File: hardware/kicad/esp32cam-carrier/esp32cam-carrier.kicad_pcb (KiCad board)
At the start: 2 copper layers, 78.7 x 33 mm, 14 parts, among them Q1 2N7000

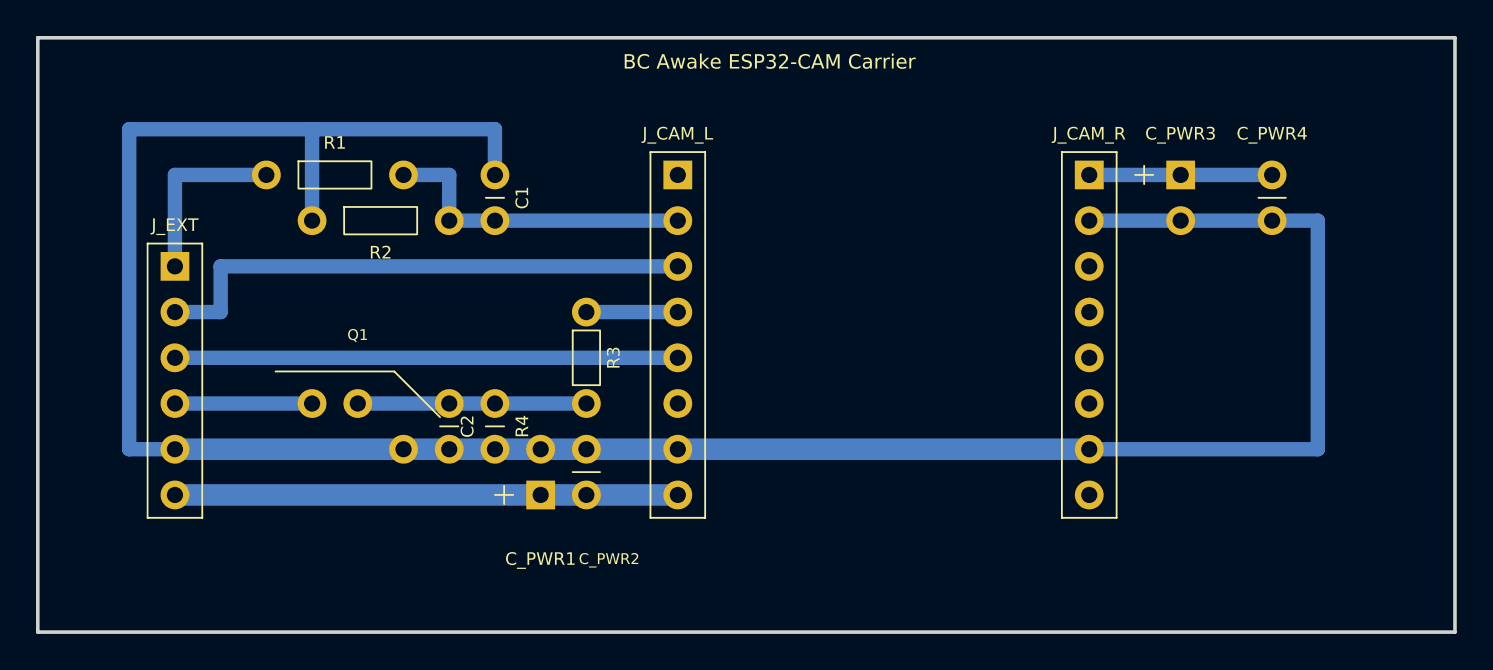
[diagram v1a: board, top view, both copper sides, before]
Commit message: fix(hardware): align ESP32-CAM carrier PCB and docs to physical pinout
- Correct ESP32-CAM ASCII header diagrams in docs/pinout.md to match physical module
- Realign J_CAM_L and J_CAM_R socket mappings and isolate IO16 (PSRAM) in scripts/generate_carrier_pcb.py
- Re-route single-layer copper B.Cu with zero track crossings and 0 DRC violations
- Update J_EXT terminal ordering and coordinate maps in docs/esp32cam-carrier-pcb.md and docs/bom.md
- Sync hardware-targets spec and archive esp32cam-prototype-pcb and fix-esp32cam-carrier-pinout changes
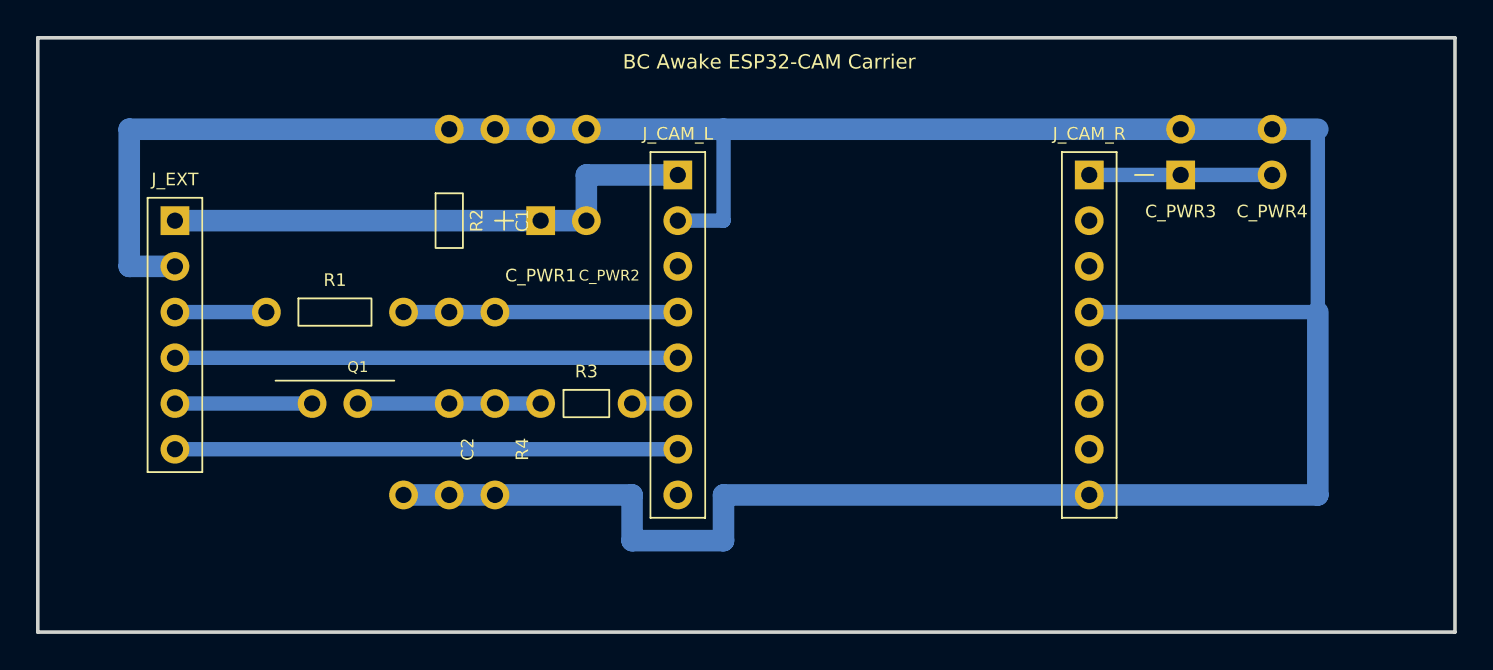
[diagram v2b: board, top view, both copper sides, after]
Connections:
- J_CAM_L pad 1: (no net) -> +5VSB
- J_CAM_L pad 2: NET_IO13 -> GND
- J_CAM_L pad 3: BTN_A -> (no net)
- J_CAM_L pad 4: NET_IO14 -> NET_IO13
- J_CAM_L pad 5: PWR_BTN# -> BTN_A
- J_CAM_L pad 6: (no net) -> NET_IO14
- J_CAM_L pad 7: GND -> PWR_BTN#
- J_CAM_L pad 8: +5VSB -> (no net)
- J_CAM_R pad 2: GND -> (no net)
- J_CAM_R pad 4: (no net) -> GND
- J_CAM_R pad 7: GND -> (no net)
- J_CAM_R pad 8: (no net) -> GND
- J_EXT pad 1: TPMS1 -> +5VSB
- J_EXT pad 2: BTN_A -> GND
- J_EXT pad 3: PWR_BTN# -> TPMS1
- J_EXT pad 4: PS_ON# -> BTN_A
- J_EXT pad 5: GND -> PS_ON#
- J_EXT pad 6: +5VSB -> PWR_BTN#
- R3 pad 1: NET_IO14 -> NET_GATE
- R3 pad 2: NET_GATE -> NET_IO14
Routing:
- net GND: track 137.2 -> 172.7 mm
- net TPMS1: track 10.2 -> 5.08 mm
- net NET_IO13: track 17.8 -> 15.2 mm
- net BTN_A: track 30.5 -> 27.9 mm
- net +5VSB: track 27.9 -> 30.5 mm
- net NET_IO14: track 5.08 -> 2.54 mm
- net NET_GATE: track 12.7 -> 10.2 mm

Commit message: fix(hardware): isolate ESP32-CAM GND/R reset pin on carrier PCB
Disconnect J_CAM_R pin 8 (GND/R) from ground to prevent holding the ESP32-CAM in hardware reset on clone boards, reroute the bottom ground bus via the left edge, and update documentation and specs.
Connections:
- J_CAM_R pad 8: GND -> (no net)
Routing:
- net GND: track 172.7 -> 139.7 mm
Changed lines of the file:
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@@
 		(pad "6" thru_hole circle (at 155.88 117.78) (size 1.6 1.6) (drill 0.9) (layers "*.Cu" "*.Mask") (net 0 ""))
 		(pad "7" thru_hole circle (at 155.88 120.32) (size 1.6 1.6) (drill 0.9) (layers "*.Cu" "*.Mask") (net 0 ""))
-		(pad "8" thru_hole circle (at 155.88 122.86) (size 1.6 1.6) (drill 0.9) (layers "*.Cu" "*.Mask") (net 1 "GND"))
+		(pad "8" thru_hole circle (at 155.88 122.86) (size 1.6 1.6) (drill 0.9) (layers "*.Cu" "*.Mask") (net 0 ""))
 	)
 	(footprint "Capacitor_THT:CP_Radial_D8.0mm_P3.50mm"
@@
 	(segment (start 168.58 102.54) (end 168.58 112.7) (width 0.8) (layer "B.Cu") (net 1))
 	(segment (start 168.58 112.7) (end 155.88 112.7) (width 0.8) (layer "B.Cu") (net 1))
-	(segment (start 168.58 112.7) (end 168.58 122.86) (width 1.2) (layer "B.Cu") (net 1))
-	(segment (start 168.58 122.86) (end 155.88 122.86) (width 1.2) (layer "B.Cu") (net 1))
-	(segment (start 155.88 122.86) (end 135.56 122.86) (width 1.2) (layer "B.Cu") (net 1))
-	(segment (start 135.56 122.86) (end 135.56 125.4) (width 1.2) (layer "B.Cu") (net 1))
-	(segment (start 135.56 125.4) (end 130.48 125.4) (width 1.2) (layer "B.Cu") (net 1))
-	(segment (start 130.48 125.4) (end 130.48 122.86) (width 1.2) (layer "B.Cu") (net 1))
-	(segment (start 130.48 122.86) (end 122.86 122.86) (width 1.2) (layer "B.Cu") (net 1))
-	(segment (start 122.86 122.86) (end 120.32 122.86) (width 1.2) (layer "B.Cu") (net 1))
-	(segment (start 120.32 122.86) (end 117.78 122.86) (width 1.2) (layer "B.Cu") (net 1))
+	(segment (start 102.54 110.16) (end 102.54 122.86) (width 1.2) (layer "B.Cu") (net 1))
+	(segment (start 102.54 122.86) (end 117.78 122.86) (width 1.2) (layer "B.Cu") (net 1))
+	(segment (start 117.78 122.86) (end 120.32 122.86) (width 1.2) (layer "B.Cu") (net 1))
+	(segment (start 120.32 122.86) (end 122.86 122.86) (width 1.2) (layer "B.Cu") (net 1))
 	(segment (start 105.08 112.7) (end 110.16 112.7) (width 0.8) (layer "B.Cu") (net 4))
 	(segment (start 117.78 112.7) (end 120.32 112.7) (width 0.8) (layer "B.Cu") (net 5))

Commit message: feat(hardware): add esp32cam-carrier target and standardize bjt buffer
- Add [env:esp32cam-carrier] build environment with BOARD_ESP32CAM_CARRIER macro
- Standardize carrier PCB switch on BC547/BC548 NPN BJT (C-B-E pinout)
- Drive active-HIGH push-pull PS_ON# and read ADC2 oversampled hysteresis on carrier board
- Restore bare ESP32-CAM target to open-drain active-LOW and digital board sense
- Regenerate KiCad schematics, PCB, netlist, DRC report, BOM, and documentation
- Sync hardware-targets and power-control specs and archive change
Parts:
- Q1: value 2N7000 -> BC547; footprint Package_TO_SOT_THT:TO-92_Inline_Wide -> Package_TO_SOT_THT:TO-92_Inline
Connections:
- Q1 pad 1: GND -> PS_ON#
- Q1 pad 3: PS_ON# -> GND
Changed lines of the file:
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@@
 		(pad "2" thru_hole circle (at 122.86 112.7) (size 1.6 1.6) (drill 0.9) (layers "*.Cu" "*.Mask") (net 5 "NET_IO13"))
 	)
-	(footprint "Package_TO_SOT_THT:TO-92_Inline_Wide"
+	(footprint "Package_TO_SOT_THT:TO-92_Inline"
 		(layer "F.Cu") (at 0 0)
 		(property "Reference" "Q1" (at 115.24 115.75 0) (layer "F.SilkS") (effects (font (size 0.6 0.6) (thickness 0.1))))
-		(property "Value" "2N7000" (at 115.24 120.32 0) (layer "F.Fab") (effects (font (size 0.6 0.6) (thickness 0.1))))
-		(fp_line (start 110.67 116.51) (end 117.27 116.51) (stroke (width 0.1) (type solid)) (layer "F.SilkS"))
-		(pad "1" thru_hole circle (at 117.78 122.86) (size 1.6 1.6) (drill 0.9) (layers "*.Cu" "*.Mask") (net 1 "GND"))
+		(property "Value" "BC547" (at 115.24 120.32 0) (layer "F.Fab") (effects (font (size 0.6 0.6) (thickness 0.1))))
+		(fp_line (start 110.67 121.59) (end 117.27 121.59) (stroke (width 0.1) (type solid)) (layer "F.SilkS"))
+		(pad "1" thru_hole circle (at 112.7 117.78) (size 1.6 1.6) (drill 0.9) (layers "*.Cu" "*.Mask") (net 6 "PS_ON#"))
 		(pad "2" thru_hole circle (at 115.24 117.78) (size 1.6 1.6) (drill 0.9) (layers "*.Cu" "*.Mask") (net 7 "NET_GATE"))
-		(pad "3" thru_hole circle (at 112.7 117.78) (size 1.6 1.6) (drill 0.9) (layers "*.Cu" "*.Mask") (net 6 "PS_ON#"))
+		(pad "3" thru_hole circle (at 117.78 122.86) (size 1.6 1.6) (drill 0.9) (layers "*.Cu" "*.Mask") (net 1 "GND"))
 	)
 	(footprint "Resistor_THT:R_Axial_DIN0207_L6.3mm_D2.5mm_P7.62mm_Horizontal"
